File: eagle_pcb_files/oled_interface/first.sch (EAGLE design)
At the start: 8 parts

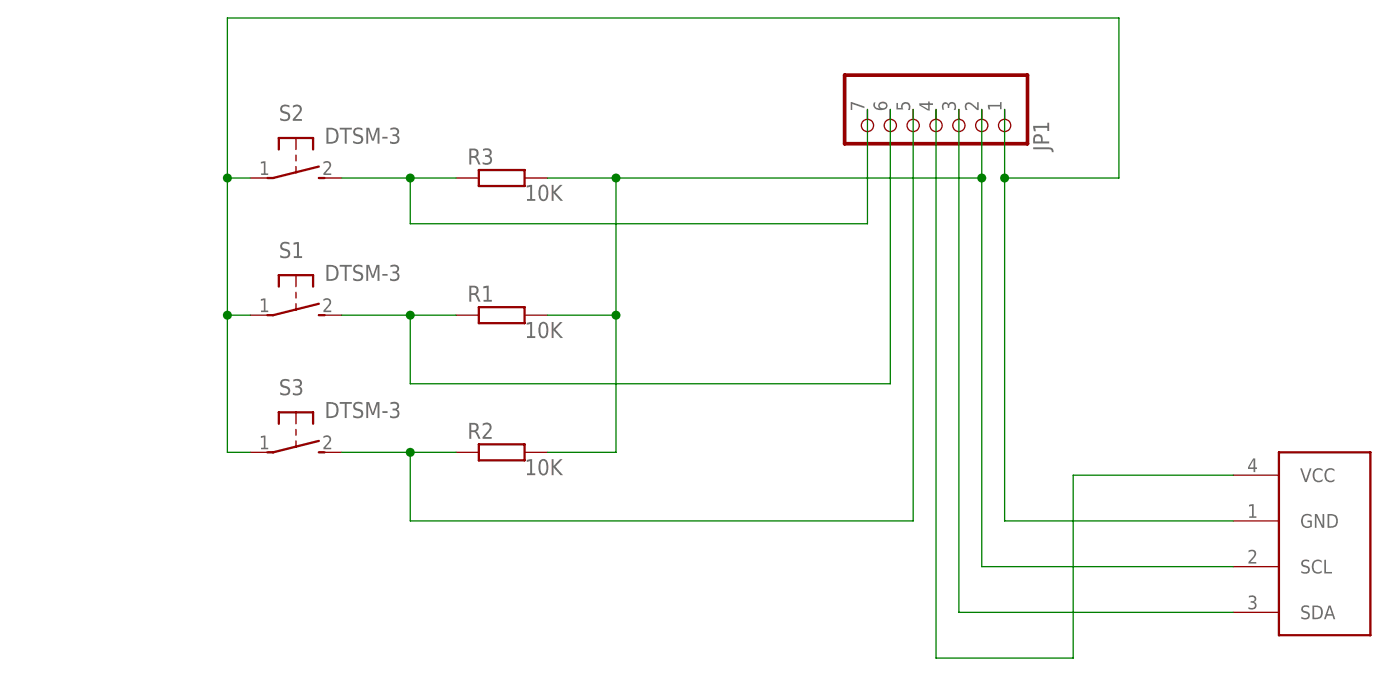
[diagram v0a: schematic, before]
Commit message: Upgraded OLED Board
New board for fast manufacturing
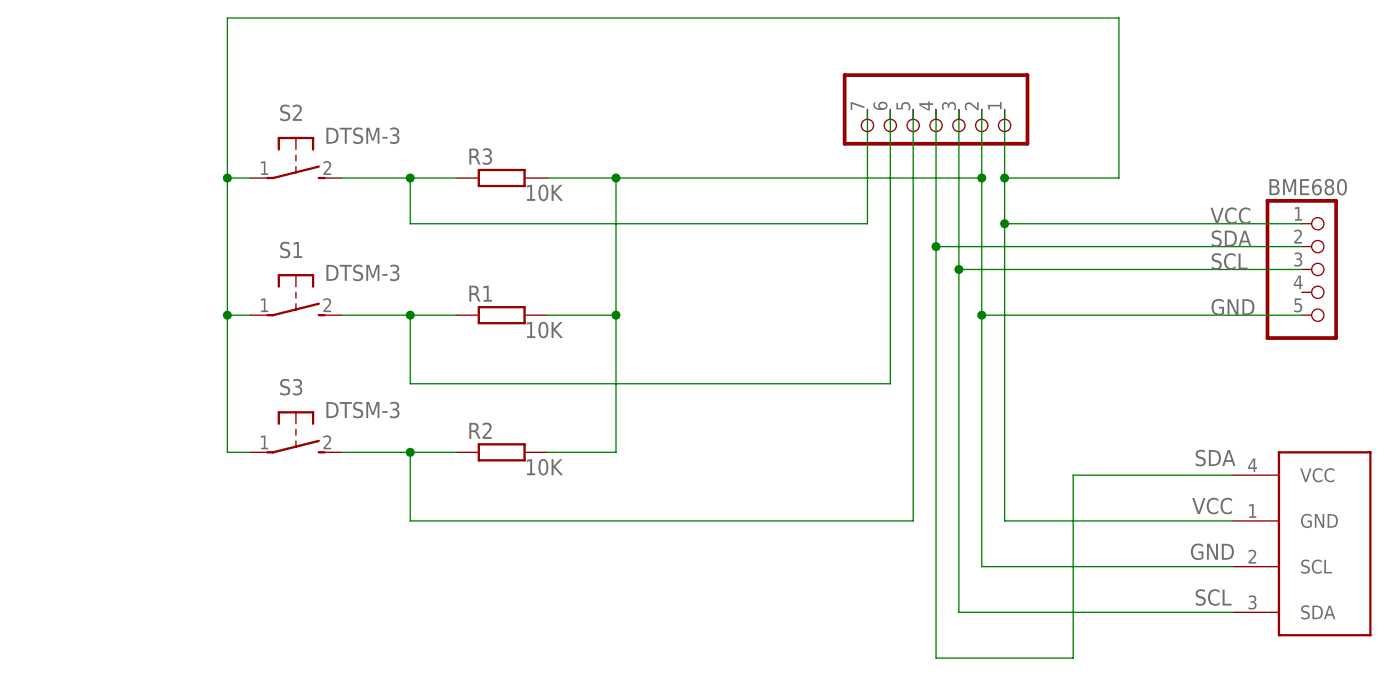
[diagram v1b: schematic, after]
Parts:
- added BME680: (no value), pinhead:PINHD-1X5
- renumbered JP1 to SDA
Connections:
- net N$5 renamed B3
- net N$6 renamed B2
- net N$7 renamed B1
- removed net N$1: R1.2, R2.2, R3.2, SDA.2, U$1.SCL
- removed net N$2: S1.1, S2.1, S3.1, SDA.1, U$1.GND
- removed net N$3: SDA.3, U$1.SDA
- new net GND: BME680.5, R1.2, R2.2, R3.2, SDA.2, U$1.SCL
- new net SCL: BME680.3, SDA.3, U$1.SDA
- new net VCC: BME680.1, S1.1, S2.1, S3.1, SDA.1, U$1.GND
- net N$4: now also BME680.2
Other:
- note added: "GND"
- note added: "SCL"
- note added: "SDA"
- note added: "VCC"
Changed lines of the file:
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@@
 <attribute name="SPICEPREFIX" value="10K"/>
 </part>
-<part name="JP1" library="pinhead" library_urn="urn:adsk.eagle:library:325" deviceset="PINHD-1X7" device="" package3d_urn="urn:adsk.eagle:package:22477/2"/>
+<part name="SDA" library="pinhead" library_urn="urn:adsk.eagle:library:325" deviceset="PINHD-1X7" device="" package3d_urn="urn:adsk.eagle:package:22477/2"/>
+<part name="BME680" library="pinhead" library_urn="urn:adsk.eagle:library:325" deviceset="PINHD-1X5" device="" package3d_urn="urn:adsk.eagle:package:22469/2"/>
 </parts>
 <sheets>
 <sheet>
 <plain>
+<text x="58.928" y="49.022" size="1.778" layer="95">VCC</text>
+<text x="58.674" y="43.942" size="1.778" layer="95">GND</text>
+<text x="59.182" y="38.862" size="1.778" layer="95">SCL</text>
+<text x="59.182" y="54.356" size="1.778" layer="95">SDA</text>
+<text x="60.96" y="71.12" size="1.778" layer="95">GND</text>
+<text x="60.96" y="76.2" size="1.778" layer="95">SCL</text>
+<text x="60.96" y="78.74" size="1.778" layer="95">SDA</text>
+<text x="60.96" y="81.28" size="1.778" layer="95">VCC</text>
 </plain>
 <instances>
@@
 <attribute name="SPICEPREFIX" x="-15.24" y="83.82" size="1.778" layer="96"/>
 </instance>
-<instance part="JP1" gate="A" x="30.48" y="91.44" smashed="yes" rot="R270">
-<attribute name="NAME" x="41.275" y="92.71" size="1.778" layer="95" rot="R270"/>
+<instance part="SDA" gate="A" x="30.48" y="91.44" smashed="yes" rot="R270">
 <attribute name="VALUE" x="17.78" y="97.79" size="1.778" layer="96" rot="R270"/>
+</instance>
+<instance part="BME680" gate="A" x="73.66" y="76.2" smashed="yes">
+<attribute name="NAME" x="67.31" y="84.455" size="1.778" layer="95"/>
+<attribute name="VALUE" x="67.31" y="66.04" size="1.778" layer="96"/>
 </instance>
 </instances>
@@
 </busses>
 <nets>
-<net name="N$3" class="0">
+<net name="SCL" class="0">
 <segment>
-<pinref part="JP1" gate="A" pin="3"/>
-<wire x1="33.02" y1="93.98" x2="33.02" y2="38.1" width="0.1524" layer="91"/>
+<pinref part="SDA" gate="A" pin="3"/>
 <pinref part="U$1" gate="G$1" pin="SDA"/>
+<wire x1="33.02" y1="93.98" x2="33.02" y2="76.2" width="0.1524" layer="91"/>
+<wire x1="33.02" y1="76.2" x2="33.02" y2="38.1" width="0.1524" layer="91"/>
 <wire x1="33.02" y1="38.1" x2="63.5" y2="38.1" width="0.1524" layer="91"/>
+<pinref part="BME680" gate="A" pin="3"/>
+<wire x1="71.12" y1="76.2" x2="33.02" y2="76.2" width="0.1524" layer="91"/>
+<junction x="33.02" y="76.2"/>
 </segment>
 </net>
 <net name="N$4" class="0">
 <segment>
-<pinref part="JP1" gate="A" pin="4"/>
-<wire x1="30.48" y1="93.98" x2="30.48" y2="33.02" width="0.1524" layer="91"/>
+<pinref part="SDA" gate="A" pin="4"/>
+<wire x1="30.48" y1="93.98" x2="30.48" y2="78.74" width="0.1524" layer="91"/>
+<wire x1="30.48" y1="78.74" x2="30.48" y2="33.02" width="0.1524" layer="91"/>
 <wire x1="30.48" y1="33.02" x2="45.72" y2="33.02" width="0.1524" layer="91"/>
 <wire x1="45.72" y1="33.02" x2="45.72" y2="53.34" width="0.1524" layer="91"/>
 <pinref part="U$1" gate="G$1" pin="VCC"/>
 <wire x1="45.72" y1="53.34" x2="63.5" y2="53.34" width="0.1524" layer="91"/>
+<pinref part="BME680" gate="A" pin="2"/>
+<wire x1="71.12" y1="78.74" x2="30.48" y2="78.74" width="0.1524" layer="91"/>
+<junction x="30.48" y="78.74"/>
 </segment>
 </net>
-<net name="N$5" class="0">
+<net name="B3" class="0">
 <segment>
 <pinref part="S2" gate="G$1" pin="2"/>
@@
 <wire x1="-27.94" y1="86.36" x2="-27.94" y2="81.28" width="0.1524" layer="91"/>
 <wire x1="-27.94" y1="81.28" x2="22.86" y2="81.28" width="0.1524" layer="91"/>
-<pinref part="JP1" gate="A" pin="7"/>
+<pinref part="SDA" gate="A" pin="7"/>
 <wire x1="22.86" y1="81.28" x2="22.86" y2="93.98" width="0.1524" layer="91"/>
 </segment>
 </net>
-<net name="N$6" class="0">
+<net name="B2" class="0">
 <segment>
 <pinref part="S1" gate="G$1" pin="2"/>
 <pinref part="R1" gate="G$1" pin="1"/>
 <wire x1="-35.56" y1="71.12" x2="-27.94" y2="71.12" width="0.1524" layer="91"/>
-<pinref part="JP1" gate="A" pin="6"/>
+<pinref part="SDA" gate="A" pin="6"/>
 <wire x1="-27.94" y1="71.12" x2="-22.86" y2="71.12" width="0.1524" layer="91"/>
 <wire x1="25.4" y1="93.98" x2="25.4" y2="63.5" width="0.1524" layer="91"/>
@@
 </segment>
 </net>
-<net name="N$7" class="0">
+<net name="B1" class="0">
 <segment>
 <pinref part="S3" gate="G$1" pin="2"/>
 <pinref part="R2" gate="G$1" pin="1"/>
 <wire x1="-35.56" y1="55.88" x2="-27.94" y2="55.88" width="0.1524" layer="91"/>
-<pinref part="JP1" gate="A" pin="5"/>
+<pinref part="SDA" gate="A" pin="5"/>
 <wire x1="-27.94" y1="55.88" x2="-22.86" y2="55.88" width="0.1524" layer="91"/>
 <wire x1="27.94" y1="93.98" x2="27.94" y2="48.26" width="0.1524" layer="91"/>
@@
 </segment>
 </net>
-<net name="N$1" class="0">
+<net name="GND" class="0">
 <segment>
 <pinref part="R3" gate="G$1" pin="2"/>
@@
 <wire x1="-12.7" y1="71.12" x2="-5.08" y2="71.12" width="0.1524" layer="91"/>
 <junction x="-5.08" y="71.12"/>
-<pinref part="JP1" gate="A" pin="2"/>
+<pinref part="SDA" gate="A" pin="2"/>
 <wire x1="35.56" y1="93.98" x2="35.56" y2="86.36" width="0.1524" layer="91"/>
-<wire x1="35.56" y1="86.36" x2="35.56" y2="43.18" width="0.1524" layer="91"/>
+<wire x1="35.56" y1="86.36" x2="35.56" y2="71.12" width="0.1524" layer="91"/>
+<wire x1="35.56" y1="71.12" x2="35.56" y2="43.18" width="0.1524" layer="91"/>
 <wire x1="-5.08" y1="86.36" x2="35.56" y2="86.36" width="0.1524" layer="91"/>
 <junction x="-5.08" y="86.36"/>
@@
 <pinref part="U$1" gate="G$1" pin="SCL"/>
 <wire x1="35.56" y1="43.18" x2="63.5" y2="43.18" width="0.1524" layer="91"/>
+<pinref part="BME680" gate="A" pin="5"/>
+<wire x1="71.12" y1="71.12" x2="35.56" y2="71.12" width="0.1524" layer="91"/>
+<junction x="35.56" y="71.12"/>
 </segment>
 </net>
-<net name="N$2" class="0">
+<net name="VCC" class="0">
 <segment>
 <pinref part="S3" gate="G$1" pin="1"/>
@@
 <wire x1="-48.26" y1="104.14" x2="50.8" y2="104.14" width="0.1524" layer="91"/>
 <wire x1="50.8" y1="104.14" x2="50.8" y2="86.36" width="0.1524" layer="91"/>
-<pinref part="JP1" gate="A" pin="1"/>
+<pinref part="SDA" gate="A" pin="1"/>
 <wire x1="38.1" y1="93.98" x2="38.1" y2="86.36" width="0.1524" layer="91"/>
-<wire x1="38.1" y1="86.36" x2="38.1" y2="48.26" width="0.1524" layer="91"/>
+<wire x1="38.1" y1="86.36" x2="38.1" y2="81.28" width="0.1524" layer="91"/>
+<wire x1="38.1" y1="81.28" x2="38.1" y2="48.26" width="0.1524" layer="91"/>
 <wire x1="50.8" y1="86.36" x2="38.1" y2="86.36" width="0.1524" layer="91"/>
 <junction x="38.1" y="86.36"/>
 <pinref part="U$1" gate="G$1" pin="GND"/>
 <wire x1="38.1" y1="48.26" x2="63.5" y2="48.26" width="0.1524" layer="91"/>
+<pinref part="BME680" gate="A" pin="1"/>
+<wire x1="71.12" y1="81.28" x2="38.1" y2="81.28" width="0.1524" layer="91"/>
+<junction x="38.1" y="81.28"/>
 </segment>
 </net>

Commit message: New Buttons Pads
previous was too small for our buttons
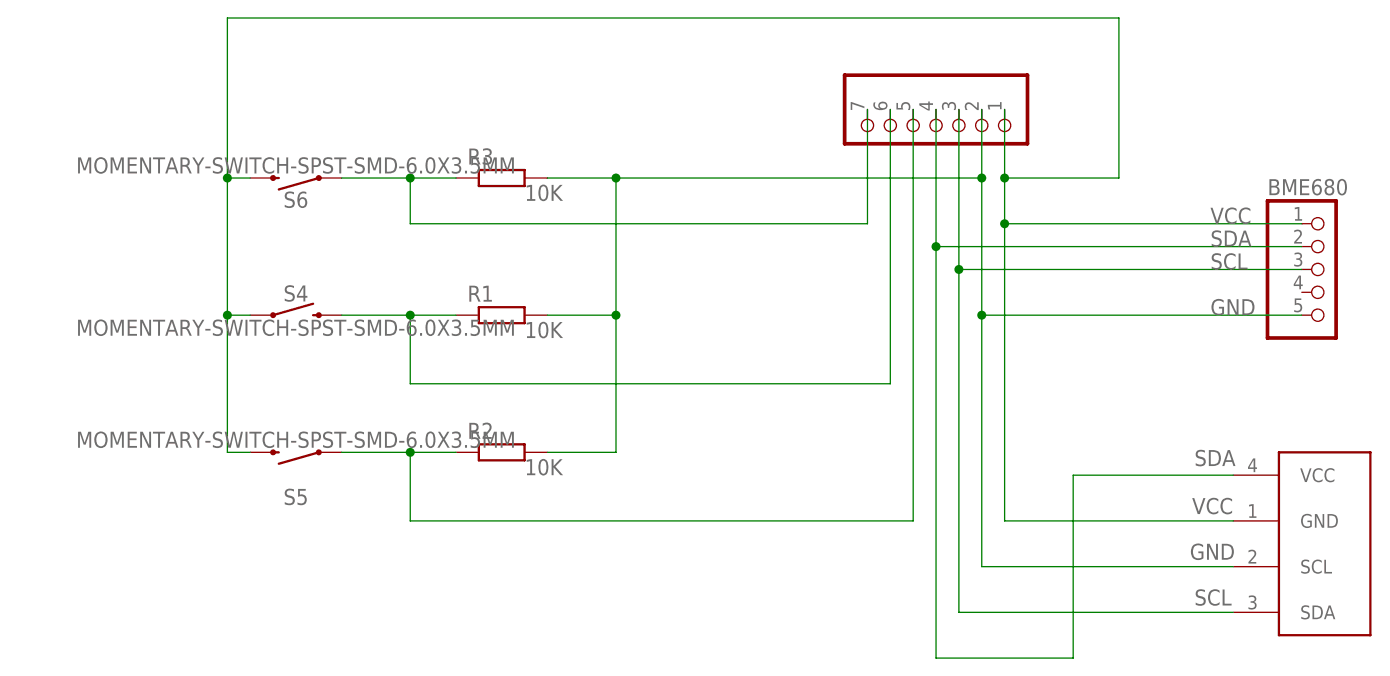
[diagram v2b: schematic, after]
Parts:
- removed S1, S2, S3: DTSM-3, switch-tact:DTSM-3
- added S4, S5, S6: MOMENTARY-SWITCH-SPST-SMD-6.0X3.5MM, SparkFun-Switches:MOMENTARY-SWITCH-SPST-SMD-6.0X3.5MM
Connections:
- net B1: now also S5.1; no longer S3.2
- net B2: now also S4.2; no longer S1.2
- net B3: now also S6.1; no longer S2.2
- net VCC: now also S4.1, S5.2, S6.2; no longer S1.1, S2.1, S3.1
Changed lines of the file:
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@@
 <parts>
 <part name="U$1" library="DIYMall_OLED" deviceset="I2C_OLED" device=""/>
-<part name="S1" library="switch-tact" deviceset="DTSM-3" device=""/>
-<part name="S2" library="switch-tact" deviceset="DTSM-3" device=""/>
-<part name="S3" library="switch-tact" deviceset="DTSM-3" device=""/>
 <part name="R1" library="rcl" library_urn="urn:adsk.eagle:library:334" deviceset="R-EU_" device="M1206" package3d_urn="urn:adsk.eagle:package:23566/1">
 <spice>
@@
 <part name="SDA" library="pinhead" library_urn="urn:adsk.eagle:library:325" deviceset="PINHD-1X7" device="" package3d_urn="urn:adsk.eagle:package:22477/2"/>
 <part name="BME680" library="pinhead" library_urn="urn:adsk.eagle:library:325" deviceset="PINHD-1X5" device="" package3d_urn="urn:adsk.eagle:package:22469/2"/>
+<part name="S4" library="SparkFun-Switches" deviceset="MOMENTARY-SWITCH-SPST" device="-SMD-6.0X3.5MM"/>
+<part name="S5" library="SparkFun-Switches" deviceset="MOMENTARY-SWITCH-SPST" device="-SMD-6.0X3.5MM"/>
+<part name="S6" library="SparkFun-Switches" deviceset="MOMENTARY-SWITCH-SPST" device="-SMD-6.0X3.5MM"/>
 </parts>
 <sheets>
@@
 <instances>
 <instance part="U$1" gate="G$1" x="106.68" y="38.1" smashed="yes"/>
-<instance part="S1" gate="G$1" x="-40.64" y="71.12" smashed="yes" rot="R270">
-<attribute name="NAME" x="-42.545" y="77.47" size="1.778" layer="95"/>
-<attribute name="VALUE" x="-37.465" y="74.93" size="1.778" layer="96"/>
-</instance>
-<instance part="S2" gate="G$1" x="-40.64" y="86.36" smashed="yes" rot="R270">
-<attribute name="NAME" x="-42.545" y="92.71" size="1.778" layer="95"/>
-<attribute name="VALUE" x="-37.465" y="90.17" size="1.778" layer="96"/>
-</instance>
-<instance part="S3" gate="G$1" x="-40.64" y="55.88" smashed="yes" rot="R270">
-<attribute name="NAME" x="-42.545" y="62.23" size="1.778" layer="95"/>
-<attribute name="VALUE" x="-37.465" y="59.69" size="1.778" layer="96"/>
-</instance>
 <instance part="R1" gate="G$1" x="-17.78" y="71.12" smashed="yes">
 <attribute name="NAME" x="-21.59" y="72.6186" size="1.778" layer="95"/>
@@
 <attribute name="NAME" x="67.31" y="84.455" size="1.778" layer="95"/>
 <attribute name="VALUE" x="67.31" y="66.04" size="1.778" layer="96"/>
+</instance>
+<instance part="S4" gate="G$1" x="-40.64" y="71.12" smashed="yes">
+<attribute name="NAME" x="-40.64" y="72.644" size="1.778" layer="95" font="vector" align="bottom-center"/>
+<attribute name="VALUE" x="-40.64" y="70.612" size="1.778" layer="96" font="vector" align="top-center"/>
+</instance>
+<instance part="S5" gate="G$1" x="-40.64" y="55.88" smashed="yes" rot="R180">
+<attribute name="NAME" x="-40.64" y="51.816" size="1.778" layer="95" font="vector" rot="R180" align="bottom-center"/>
+<attribute name="VALUE" x="-40.64" y="56.388" size="1.778" layer="96" font="vector" rot="R180" align="top-center"/>
+</instance>
+<instance part="S6" gate="G$1" x="-40.64" y="86.36" smashed="yes" rot="R180">
+<attribute name="NAME" x="-40.64" y="84.836" size="1.778" layer="95" font="vector" rot="R180" align="bottom-center"/>
+<attribute name="VALUE" x="-40.64" y="86.868" size="1.778" layer="96" font="vector" rot="R180" align="top-center"/>
 </instance>
 </instances>
@@
 <net name="B3" class="0">
 <segment>
-<pinref part="S2" gate="G$1" pin="2"/>
 <pinref part="R3" gate="G$1" pin="1"/>
 <wire x1="-35.56" y1="86.36" x2="-27.94" y2="86.36" width="0.1524" layer="91"/>
@@
 <pinref part="SDA" gate="A" pin="7"/>
 <wire x1="22.86" y1="81.28" x2="22.86" y2="93.98" width="0.1524" layer="91"/>
+<pinref part="S6" gate="G$1" pin="1"/>
 </segment>
 </net>
 <net name="B2" class="0">
 <segment>
-<pinref part="S1" gate="G$1" pin="2"/>
 <pinref part="R1" gate="G$1" pin="1"/>
-<wire x1="-35.56" y1="71.12" x2="-27.94" y2="71.12" width="0.1524" layer="91"/>
 <pinref part="SDA" gate="A" pin="6"/>
 <wire x1="-27.94" y1="71.12" x2="-22.86" y2="71.12" width="0.1524" layer="91"/>
@@
 <wire x1="-27.94" y1="63.5" x2="-27.94" y2="71.12" width="0.1524" layer="91"/>
 <junction x="-27.94" y="71.12"/>
+<pinref part="S4" gate="G$1" pin="2"/>
+<wire x1="-35.56" y1="71.12" x2="-27.94" y2="71.12" width="0.1524" layer="91"/>
 </segment>
 </net>
 <net name="B1" class="0">
 <segment>
-<pinref part="S3" gate="G$1" pin="2"/>
 <pinref part="R2" gate="G$1" pin="1"/>
-<wire x1="-35.56" y1="55.88" x2="-27.94" y2="55.88" width="0.1524" layer="91"/>
 <pinref part="SDA" gate="A" pin="5"/>
 <wire x1="-27.94" y1="55.88" x2="-22.86" y2="55.88" width="0.1524" layer="91"/>
@@
 <wire x1="-27.94" y1="48.26" x2="-27.94" y2="55.88" width="0.1524" layer="91"/>
 <junction x="-27.94" y="55.88"/>
+<pinref part="S5" gate="G$1" pin="1"/>
+<wire x1="-27.94" y1="55.88" x2="-35.56" y2="55.88" width="0.1524" layer="91"/>
 </segment>
 </net>
@@
 <net name="VCC" class="0">
 <segment>
-<pinref part="S3" gate="G$1" pin="1"/>
-<wire x1="-45.72" y1="55.88" x2="-48.26" y2="55.88" width="0.1524" layer="91"/>
 <wire x1="-48.26" y1="55.88" x2="-48.26" y2="71.12" width="0.1524" layer="91"/>
-<pinref part="S1" gate="G$1" pin="1"/>
-<wire x1="-48.26" y1="71.12" x2="-45.72" y2="71.12" width="0.1524" layer="91"/>
 <wire x1="-48.26" y1="71.12" x2="-48.26" y2="86.36" width="0.1524" layer="91"/>
 <junction x="-48.26" y="71.12"/>
-<pinref part="S2" gate="G$1" pin="1"/>
-<wire x1="-48.26" y1="86.36" x2="-45.72" y2="86.36" width="0.1524" layer="91"/>
 <wire x1="-48.26" y1="86.36" x2="-48.26" y2="104.14" width="0.1524" layer="91"/>
 <junction x="-48.26" y="86.36"/>
@@
 <wire x1="71.12" y1="81.28" x2="38.1" y2="81.28" width="0.1524" layer="91"/>
 <junction x="38.1" y="81.28"/>
-</segment>
-</net>
+<pinref part="S6" gate="G$1" pin="2"/>
+<pinref part="S4" gate="G$1" pin="1"/>
+<pinref part="S5" gate="G$1" pin="2"/>
+<wire x1="-48.26" y1="55.88" x2="-45.72" y2="55.88" width="0.1524" layer="91"/>
+<wire x1="-48.26" y1="71.12" x2="-45.72" y2="71.12" width="0.1524" layer="91"/>
+<wire x1="-48.26" y1="86.36" x2="-45.72" y2="86.36" width="0.1524" layer="91"/>
+</segment>
+</net>
